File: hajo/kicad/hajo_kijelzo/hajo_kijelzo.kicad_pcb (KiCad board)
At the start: 2 copper layers, 62 x 92 mm, 21 parts, among them J1 SeaTalk NG, J2 Debug, J3 Fuel, J5 Water, J6 Display, Q1 BC557, U1 MCP2562, U2 LF50CV, U3 LF33_TO220, U4 WeMos_S2_mini

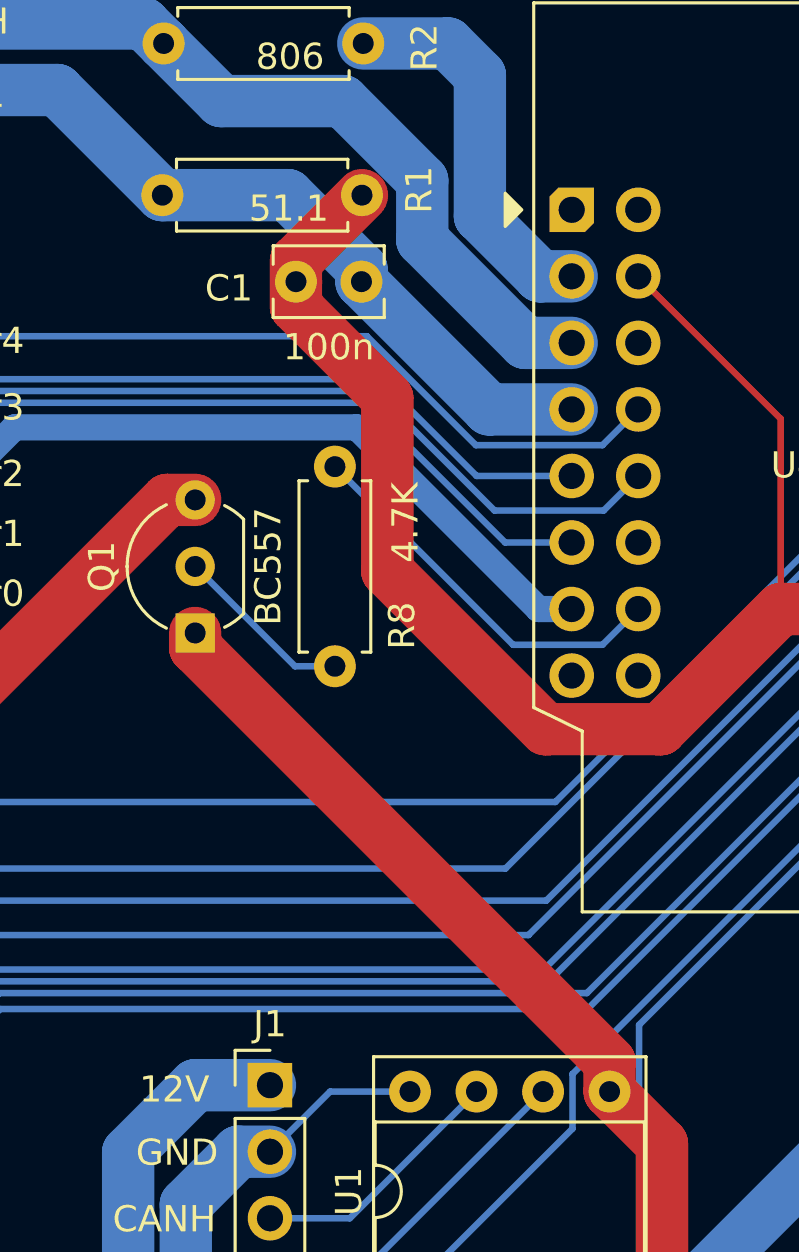
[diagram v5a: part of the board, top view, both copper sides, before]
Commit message: add back CanStby
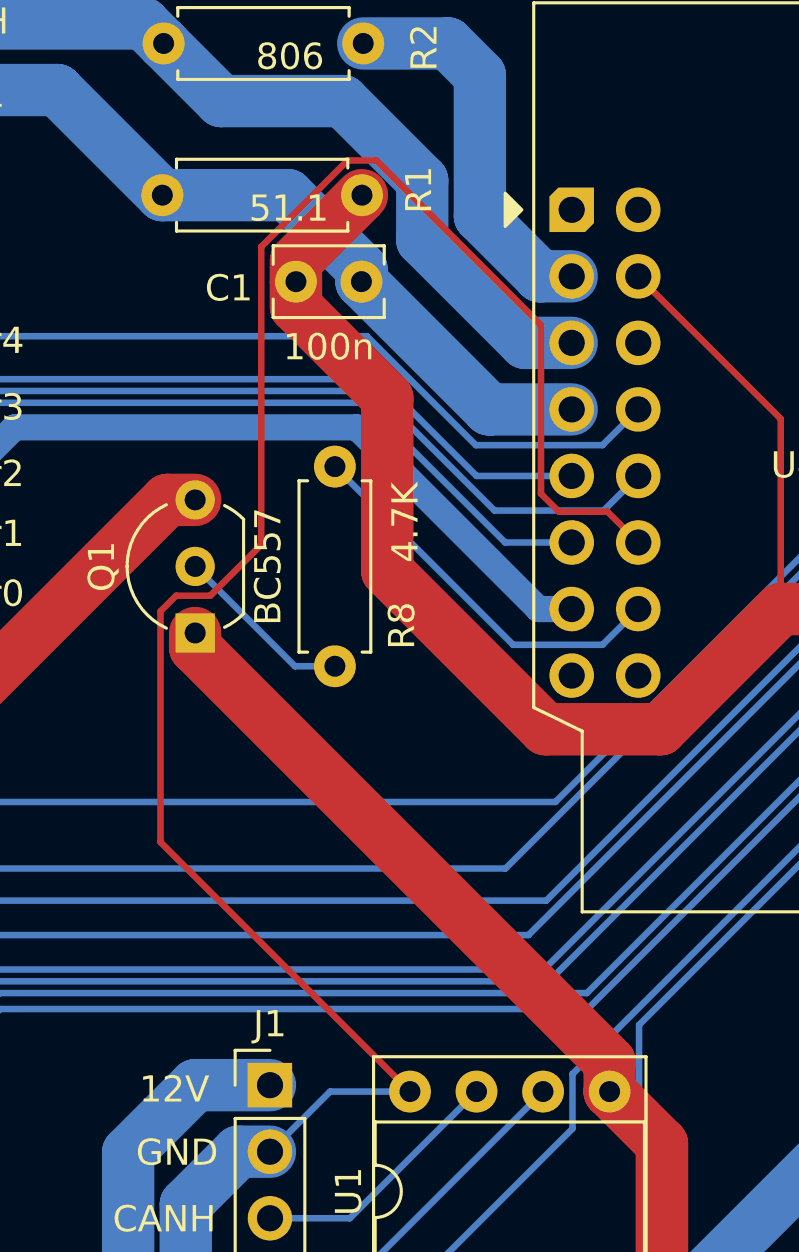
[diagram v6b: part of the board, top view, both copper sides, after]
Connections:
- U1 pad 8: GND -> /CanStby
- U4 pad 22: unconnected-(U4-GPIO10-Pad22) -> /CanStby
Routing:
- net /CanStby: track 0.00 -> 64.1 mm
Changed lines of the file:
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@@
   (net 34 "unconnected-(U4-GPIO15-Pad25)")
   (net 35 "unconnected-(U4-GPIO4-Pad19)")
-  (net 36 "unconnected-(U4-GPIO10-Pad22)")
+  (net 36 "/CanStby")
   (net 37 "unconnected-(U4-GPIO1-Pad17)")
   (footprint "Capacitor_THT:C_Rect_L7.0mm_W2.0mm_P5.00mm" (layer "F.Cu")
@@
       (net 25 "/Water2") (pinfunction "GPIO8") (pintype "bidirectional"))
     (pad "22" thru_hole circle (at 2.54 12.7) (size 1.7 1.7) (drill 1) (layers "*.Cu" "*.Mask")
-      (net 36 "unconnected-(U4-GPIO10-Pad22)") (pinfunction "GPIO10") (pintype "bidirectional+no_connect"))
+      (net 36 "/CanStby") (pinfunction "GPIO10") (pintype "bidirectional"))
     (pad "23" thru_hole circle (at 2.54 15.24) (size 1.7 1.7) (drill 1) (layers "*.Cu" "*.Mask")
       (net 28 "/LED") (pinfunction "GPIO13") (pintype "bidirectional"))
@@
       (net 3 "/CANH") (pinfunction "CANH") (pintype "bidirectional"))
     (pad "8" thru_hole oval (at 7.62 0 90) (size 1.6 1.6) (drill 0.8) (layers "*.Cu" "*.Mask")
-      (net 4 "GND") (pinfunction "STBY") (pintype "input"))
+      (net 36 "/CanStby") (pinfunction "STBY") (pintype "input"))
     (model "${KICAD6_3DMODEL_DIR}/Package_DIP.3dshapes/DIP-8_W7.62mm_Socket.wrl"
       (offset (xyz 0 0 0))
@@
   (segment (start 74.776 60.442) (end 72.902167 60.442) (width 0.25) (layer "B.Cu") (net 30))
   (segment (start 72.902167 60.442) (end 55.702 77.642167) (width 0.25) (layer "B.Cu") (net 30))
+  (segment (start 52.644299 58.052) (end 54.496 58.052) (width 0.25) (layer "F.Cu") (net 36))
+  (segment (start 45.673432 44.6432) (end 51.956 50.925768) (width 0.25) (layer "F.Cu") (net 36))
+  (segment (start 51.956 50.925768) (end 51.956 57.363701) (width 0.25) (layer "F.Cu") (net 36))
+  (segment (start 38.029 61.259) (end 39.3342 61.259) (width 0.25) (layer "F.Cu") (net 36))
+  (segment (start 46.957 80.187) (end 37.432 70.662) (width 0.25) (layer "F.Cu") (net 36))
+  (segment (start 37.432 61.856) (end 38.029 61.259) (width 0.25) (layer "F.Cu") (net 36))
+  (segment (start 44.575768 44.6432) (end 45.673432 44.6432) (width 0.25) (layer "F.Cu") (net 36))
+  (segment (start 39.3342 61.259) (end 41.2796 59.3136) (width 0.25) (layer "F.Cu") (net 36))
+  (segment (start 41.2796 59.3136) (end 41.2796 47.939368) (width 0.25) (layer "F.Cu") (net 36))
+  (segment (start 37.432 70.662) (end 37.432 61.856) (width 0.25) (layer "F.Cu") (net 36))
+  (segment (start 51.956 57.363701) (end 52.644299 58.052) (width 0.25) (layer "F.Cu") (net 36))
+  (segment (start 41.2796 47.939368) (end 44.575768 44.6432) (width 0.25) (layer "F.Cu") (net 36))
+  (segment (start 54.496 58.052) (end 55.671 59.227) (width 0.25) (layer "F.Cu") (net 36))
 )

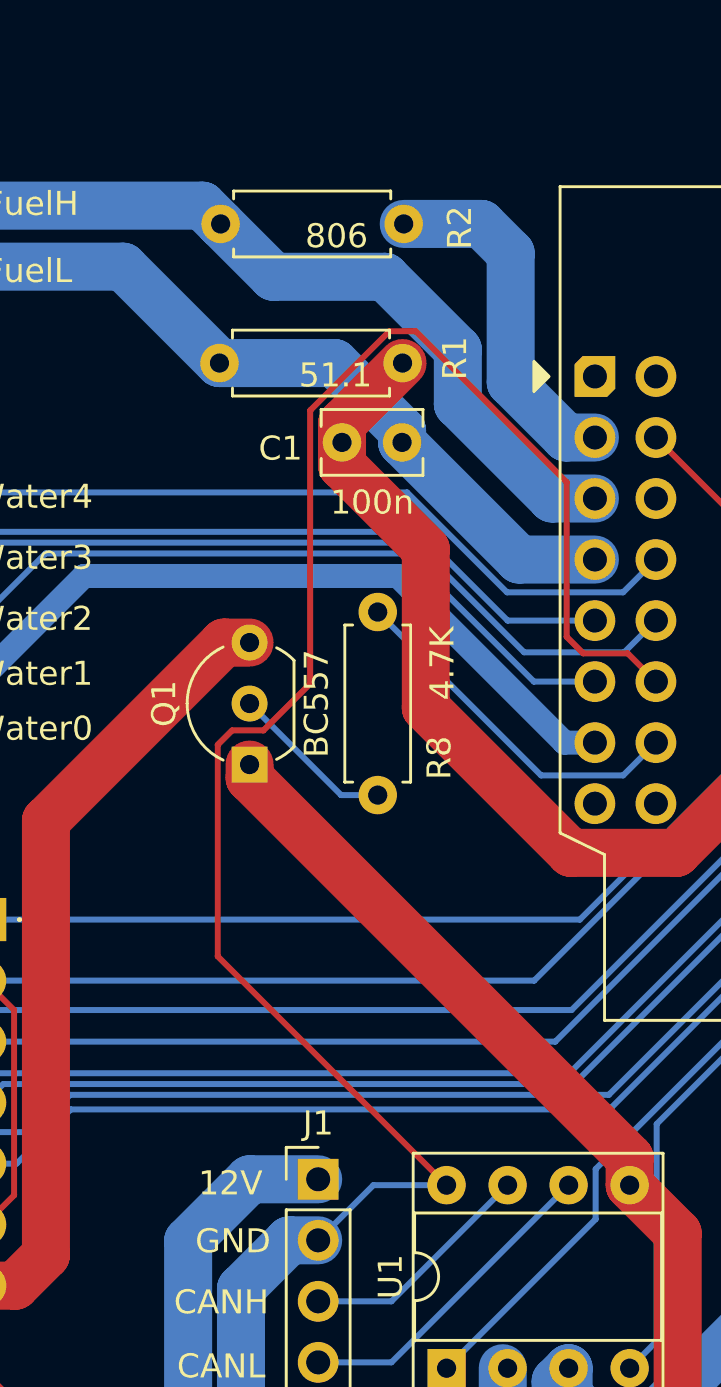
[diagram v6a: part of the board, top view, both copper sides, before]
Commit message: fix mcp2562 pins
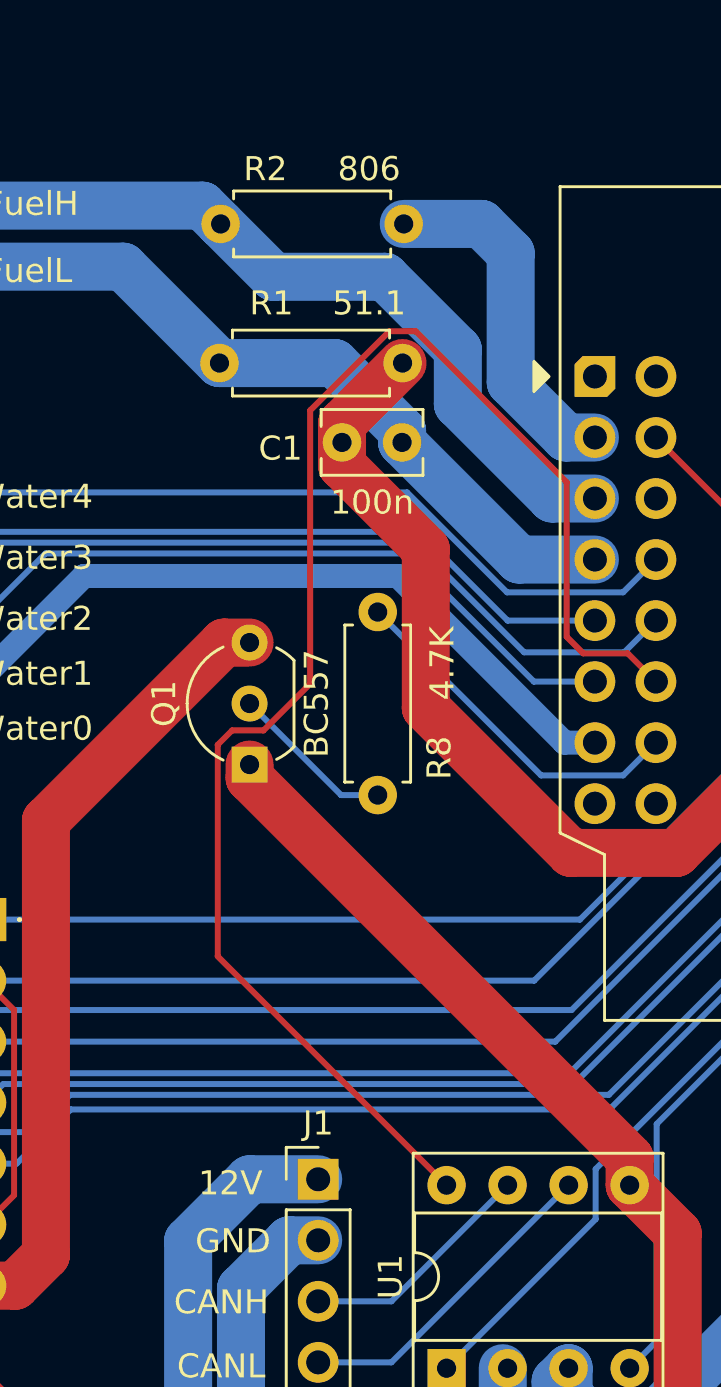
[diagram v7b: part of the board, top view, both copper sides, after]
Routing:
- net GND: track 281.2 -> 274.9 mm
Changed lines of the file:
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@@
     (property "ki_keywords" "R res resistor")
     (attr through_hole)
-    (fp_text reference "R1" (at -2.182 0.2028 90) (layer "F.SilkS")
-        (effects (font (size 1 1) (thickness 0.15)))
-    )
-    (fp_text value "51.1" (at 2.794 -0.508) (layer "F.SilkS")
+    (fp_text reference "R1" (at 5.4556 2.4892 180) (layer "F.SilkS")
+        (effects (font (size 1 1) (thickness 0.15)))
+    )
+    (fp_text value "51.1" (at 1.3916 2.4892) (layer "F.SilkS")
         (effects (font (size 1 1) (thickness 0.15)))
     )
@@
     (property "ki_keywords" "R res resistor")
     (attr through_hole)
-    (fp_text reference "R2" (at -2.3344 -0.1528 90) (layer "F.SilkS")
-        (effects (font (size 1 1) (thickness 0.15)))
-    )
-    (fp_text value "806" (at 2.794 -0.508) (layer "F.SilkS")
+    (fp_text reference "R2" (at 5.758 2.2864 180) (layer "F.SilkS")
+        (effects (font (size 1 1) (thickness 0.15)))
+    )
+    (fp_text value "806" (at 1.44 2.2864) (layer "F.SilkS")
         (effects (font (size 1 1) (thickness 0.15)))
     )
@@
   (segment (start 40.410919 82.483) (end 38.399 84.494919) (width 2) (layer "B.Cu") (net 4))
   (segment (start 38.399 90.723) (end 38.399 93.2285) (width 2) (layer "B.Cu") (net 4))
-  (segment (start 43.909 80.187) (end 41.613 82.483) (width 0.25) (layer "B.Cu") (net 4))
   (segment (start 75.991 61.767) (end 77.193081 61.767) (width 2) (layer "B.Cu") (net 4))
   (segment (start 77.193081 61.767) (end 78.531 60.429081) (width 2) (layer "B.Cu") (net 4))
@@
   (segment (start 54.575 104.073) (end 56.575 104.073) (width 2) (layer "B.Cu") (net 4))
   (segment (start 23.091 82.155001) (end 23.413001 81.833) (width 2) (layer "B.Cu") (net 4))
-  (segment (start 46.957 80.187) (end 43.909 80.187) (width 0.25) (layer "B.Cu") (net 4))
   (segment (start 40.065 96.707) (end 40.065 97.27827) (width 2) (layer "B.Cu") (net 4))
   (segment (start 38.399 90.723) (end 48.041 90.723) (width 2) (layer "B.Cu") (net 4))
